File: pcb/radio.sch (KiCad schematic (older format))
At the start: 20 parts, among them IC401 Si4460, P401 COAX

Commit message: Work on schematic
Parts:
- removed Y?: TCXO 25MHz, Jerboa:ASTX_H11, symbol agg-kicad:TCXO
- added R? (x2): 100, symbol agg-kicad:R
- added R?: 68, symbol agg-kicad:R
- added R? (x2): 4k7, symbol agg-kicad:R
- added Y?: TCXO, Jerboa:ASTX_H11, symbol ASTX_H11:TCXO
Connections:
- net labels added: SI5351_3V3, WSPR_SCL, WSPR_SDA
- wire segments 44 -> 68
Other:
- moved on the sheet: U?
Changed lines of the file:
@@
 	6800 1850 7100 1850
-$Comp
-L agg-kicad:TCXO Y?
-U 1 1 5A7CB0D5
-P 3450 3850
-F 0 "Y?" H 3450 4075 50  0000 C CNN
-F 1 "TCXO 25MHz" H 3450 3984 50  0000 C CNN
-F 2 "Jerboa:ASTX_H11" H 3250 3850 50  0001 C CNN
-F 3 "" H 3250 3850 50  0001 C CNN
-F 4 "535-12039-1-ND" H 3450 3850 60  0001 C CNN "Digikey"
-	1    3450 3850
-	1    0    0    -1
-$EndComp
 $Comp
 L SI5351A_10_pin:SI5351A_10_pin U?
 U 1 1 5A7CC074
-P 4250 4200
-F 0 "U?" H 4750 4447 60  0000 C CNN
-F 1 "SI5351A_10_pin" H 4750 4341 60  0000 C CNN
-F 2 "" H 4250 4200 60  0001 C CNN
-F 3 "" H 4250 4200 60  0001 C CNN
-	1    4250 4200
+P 6600 4400
+F 0 "U?" H 7100 4647 60  0000 C CNN
+F 1 "SI5351A_10_pin" H 7100 4541 60  0000 C CNN
+F 2 "" H 6600 4400 60  0001 C CNN
+F 3 "" H 6600 4400 60  0001 C CNN
+	1    6600 4400
 	1    0    0    -1
 $EndComp
@@
 	1    0    0    -1
 $EndComp
+Text Label 6500 4350 2    60   ~ 0
+SI5351_3V3
+Text Label 2700 4100 0    60   ~ 0
+SI5351_3V3
+$Comp
+L ASTX_H11:TCXO Y?
+U 1 1 5A85FAB2
+P 5250 4800
+F 0 "Y?" H 5250 5025 50  0000 C CNN
+F 1 "TCXO" H 5250 4934 50  0000 C CNN
+F 2 "Jerboa:ASTX_H11" H 5250 4400 50  0001 C CNN
+F 3 "http://www.abracon.com/Oscillators/ASTX-H11.pdf" H 5250 4450 50  0001 C CNN
+F 4 "535-12039-1-ND" H 5050 4500 50  0001 L CNN "Digikey"
+	1    5250 4800
+	1    0    0    -1
+$EndComp
+Text Label 4900 4800 2    60   ~ 0
+SI5351_3V3
+Wire Wire Line
+	4900 4800 4950 4800
+Text Label 5650 5000 3    60   ~ 0
+SI5351_3V3
+$Comp
+L agg-kicad:R R?
+U 1 1 5A866FF6
+P 6200 4650
+F 0 "R?" V 6204 4691 50  0000 L CNN
+F 1 "100" V 6295 4691 50  0000 L CNN
+F 2 "" H 6200 4650 50  0001 C CNN
+F 3 "" H 6200 4650 50  0001 C CNN
+F 4 "Value" H 6200 4650 60  0001 C CNN "Farnell"
+	1    6200 4650
+	0    1    1    0
+$EndComp
+$Comp
+L agg-kicad:R R?
+U 1 1 5A867144
+P 6000 4800
+F 0 "R?" H 6050 4622 50  0000 C CNN
+F 1 "68" H 6050 4713 50  0000 C CNN
+F 2 "" H 6000 4800 50  0001 C CNN
+F 3 "" H 6000 4800 50  0001 C CNN
+F 4 "Value" H 6000 4800 60  0001 C CNN "Farnell"
+	1    6000 4800
+	-1   0    0    1
+$EndComp
+$Comp
+L agg-kicad:R R?
+U 1 1 5A8671A3
+P 5650 4650
+F 0 "R?" V 5654 4691 50  0000 L CNN
+F 1 "100" V 5745 4691 50  0000 L CNN
+F 2 "" H 5650 4650 50  0001 C CNN
+F 3 "" H 5650 4650 50  0001 C CNN
+F 4 "Value" H 5650 4650 60  0001 C CNN "Farnell"
+	1    5650 4650
+	0    1    1    0
+$EndComp
+Wire Wire Line
+	5550 4800 5900 4800
+Wire Wire Line
+	6000 4800 6600 4800
+Wire Wire Line
+	5650 4750 5650 4800
+Connection ~ 5650 4800
+Wire Wire Line
+	6200 4750 6200 4800
+Connection ~ 6200 4800
+Wire Wire Line
+	5550 4900 6600 4900
+$Comp
+L agg-kicad:GND #PWR?
+U 1 1 5A870B99
+P 5650 4600
+F 0 "#PWR?" H 5520 4640 50  0001 L CNN
+F 1 "GND" H 5650 4500 50  0000 C CNN
+F 2 "" H 5650 4600 60  0000 C CNN
+F 3 "" H 5650 4600 60  0000 C CNN
+	1    5650 4600
+	-1   0    0    1
+$EndComp
+$Comp
+L agg-kicad:GND #PWR?
+U 1 1 5A870C94
+P 6200 4600
+F 0 "#PWR?" H 6070 4640 50  0001 L CNN
+F 1 "GND" H 6200 4500 50  0000 C CNN
+F 2 "" H 6200 4600 60  0000 C CNN
+F 3 "" H 6200 4600 60  0000 C CNN
+	1    6200 4600
+	-1   0    0    1
+$EndComp
+Wire Wire Line
+	6200 4600 6200 4650
+Wire Wire Line
+	5650 4600 5650 4650
+$Comp
+L agg-kicad:GND #PWR?
+U 1 1 5A8745C5
+P 4900 4950
+F 0 "#PWR?" H 4770 4990 50  0001 L CNN
+F 1 "GND" H 4900 4850 50  0000 C CNN
+F 2 "" H 4900 4950 60  0000 C CNN
+F 3 "" H 4900 4950 60  0000 C CNN
+	1    4900 4950
+	1    0    0    -1
+$EndComp
+Wire Wire Line
+	4900 4950 4900 4900
+Wire Wire Line
+	4900 4900 4950 4900
+Wire Wire Line
+	6600 4500 6550 4500
+Wire Wire Line
+	6550 4350 6550 4500
+Wire Wire Line
+	6550 4400 6600 4400
+$Comp
+L agg-kicad:GND #PWR?
+U 1 1 5A8787FE
+P 6550 4650
+F 0 "#PWR?" H 6420 4690 50  0001 L CNN
+F 1 "GND" H 6550 4550 50  0000 C CNN
+F 2 "" H 6550 4650 60  0000 C CNN
+F 3 "" H 6550 4650 60  0000 C CNN
+	1    6550 4650
+	1    0    0    -1
+$EndComp
+Wire Wire Line
+	6550 4650 6550 4600
+Wire Wire Line
+	6550 4600 6600 4600
+Wire Wire Line
+	6500 4350 6550 4350
+Connection ~ 6550 4400
+$Comp
+L agg-kicad:R R?
+U 1 1 5A884D06
+P 6400 4950
+F 0 "R?" V 6404 4991 50  0000 L CNN
+F 1 "4k7" V 6495 4991 50  0000 L CNN
+F 2 "" H 6400 4950 50  0001 C CNN
+F 3 "" H 6400 4950 50  0001 C CNN
+F 4 "Value" H 6400 4950 60  0001 C CNN "Farnell"
+	1    6400 4950
+	0    1    1    0
+$EndComp
+$Comp
+L agg-kicad:R R?
+U 1 1 5A884DE4
+P 6400 5250
+F 0 "R?" V 6404 5291 50  0000 L CNN
+F 1 "4k7" V 6495 5291 50  0000 L CNN
+F 2 "" H 6400 5250 50  0001 C CNN
+F 3 "" H 6400 5250 50  0001 C CNN
+F 4 "Value" H 6400 5250 60  0001 C CNN "Farnell"
+	1    6400 5250
+	0    1    1    0
+$EndComp
+Wire Wire Line
+	6200 5100 6600 5100
+Connection ~ 6400 5100
+Wire Wire Line
+	6200 5200 6600 5200
+Connection ~ 6400 5200
+Wire Wire Line
+	6400 5050 6400 5100
+Wire Wire Line
+	5650 4950 6400 4950
+Wire Wire Line
+	6400 5250 6400 5200
+Wire Wire Line
+	6350 5350 6400 5350
+Text Label 6200 5200 2    60   ~ 0
+WSPR_SDA
+Text Label 6200 5100 2    60   ~ 0
+WSPR_SCL
+Wire Wire Line
+	5650 5000 5650 4900
+Connection ~ 5650 4900
+Connection ~ 5650 4950
+Wire Wire Line
+	6350 5350 6350 4950
+Connection ~ 6350 4950
 $EndSCHEMATC

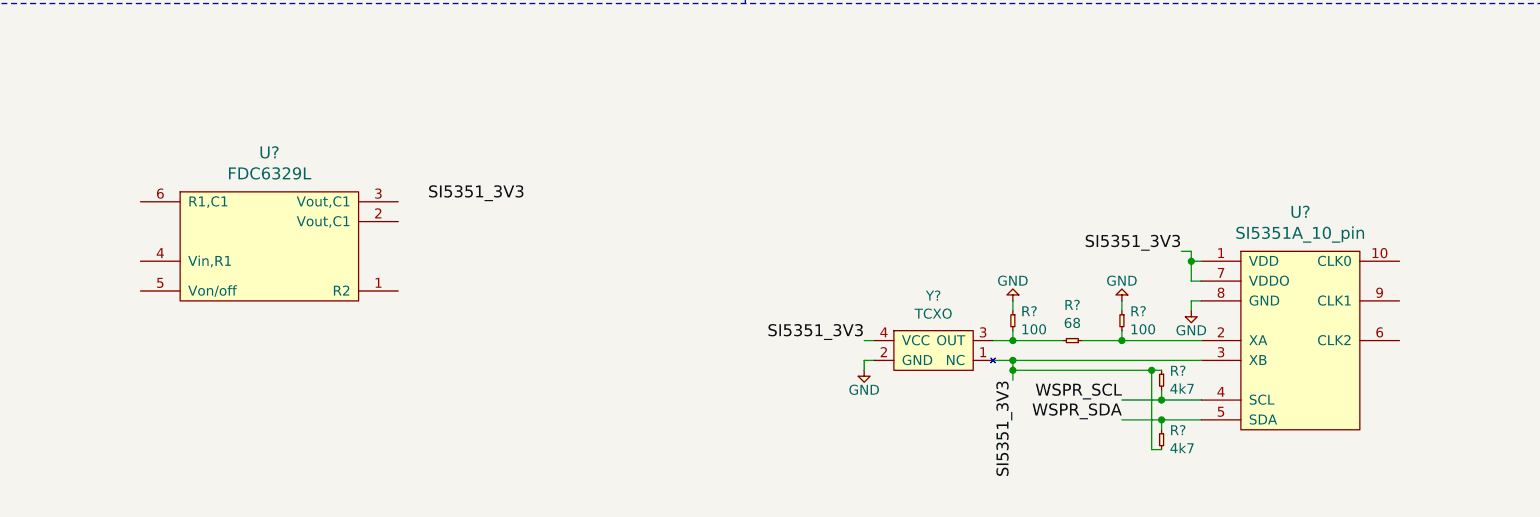
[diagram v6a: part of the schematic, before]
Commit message: Add wspr breakout board and reorganise sub project libraries
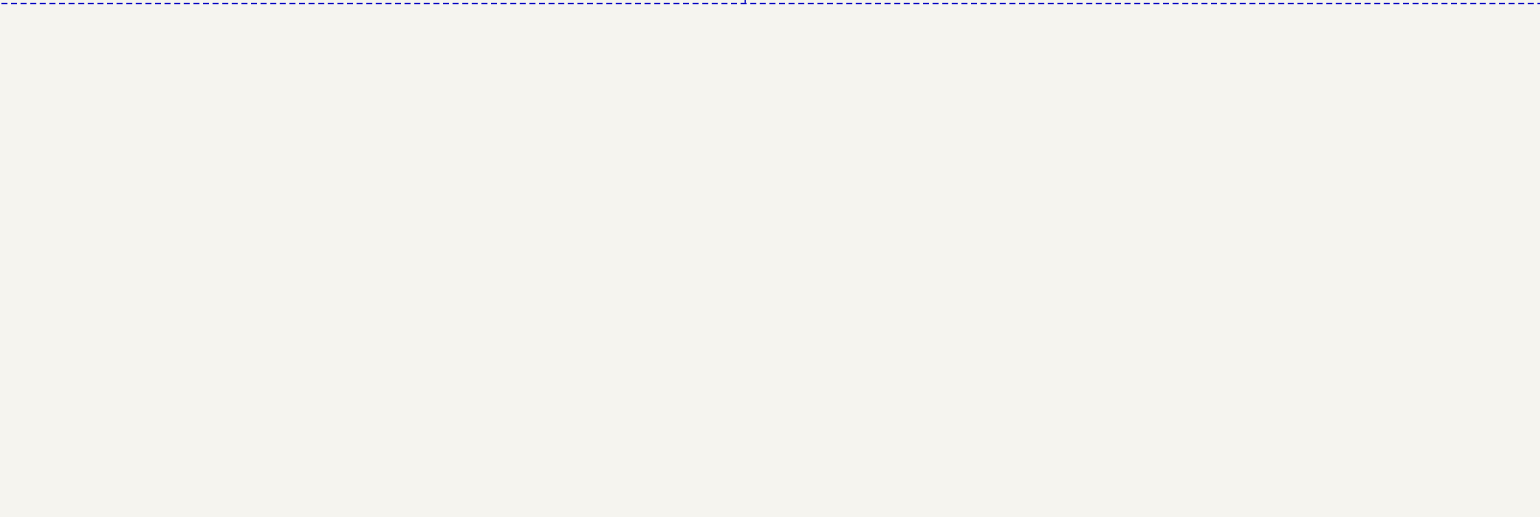
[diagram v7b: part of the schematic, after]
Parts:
- removed R? (x2): 100, symbol agg-kicad:R
- removed R?: 68, symbol agg-kicad:R
- removed R? (x2): 4k7, symbol agg-kicad:R
- removed U?: SI5351A_10_pin, symbol SI5351A_10_pin:SI5351A_10_pin
- removed U?: FDC6329L, Jerboa:SuperSOT-6, symbol FDC6329L:FDC6329L
- removed Y?: TCXO, Jerboa:ASTX_H11, symbol ASTX_H11:TCXO
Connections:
- net labels removed: SI5351_3V3, WSPR_SCL, WSPR_SDA
- wire segments 68 -> 44
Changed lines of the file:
@@
 Wire Wire Line
 	6800 1850 7100 1850
-$Comp
-L SI5351A_10_pin:SI5351A_10_pin U?
-U 1 1 5A7CC074
-P 6600 4400
-F 0 "U?" H 7100 4647 60  0000 C CNN
-F 1 "SI5351A_10_pin" H 7100 4541 60  0000 C CNN
-F 2 "" H 6600 4400 60  0001 C CNN
-F 3 "" H 6600 4400 60  0001 C CNN
-	1    6600 4400
-	1    0    0    -1
-$EndComp
-$Comp
-L FDC6329L:FDC6329L U?
-U 1 1 5A7E3431
-P 1900 4200
-F 0 "U?" H 1900 4547 60  0000 C CNN
-F 1 "FDC6329L" H 1900 4441 60  0000 C CNN
-F 2 "Jerboa:SuperSOT-6" H 1900 3550 60  0001 C CNN
-F 3 "http://www.farnell.com/datasheets/2285836.pdf" H 1900 3650 60  0001 C CNN
-F 4 "1652469" H 1900 3450 60  0001 C CNN "Farnell"
-	1    1900 4200
-	1    0    0    -1
-$EndComp
-Text Label 6500 4350 2    60   ~ 0
-SI5351_3V3
-Text Label 2700 4100 0    60   ~ 0
-SI5351_3V3
-$Comp
-L ASTX_H11:TCXO Y?
-U 1 1 5A85FAB2
-P 5250 4800
-F 0 "Y?" H 5250 5025 50  0000 C CNN
-F 1 "TCXO" H 5250 4934 50  0000 C CNN
-F 2 "Jerboa:ASTX_H11" H 5250 4400 50  0001 C CNN
-F 3 "http://www.abracon.com/Oscillators/ASTX-H11.pdf" H 5250 4450 50  0001 C CNN
-F 4 "535-12039-1-ND" H 5050 4500 50  0001 L CNN "Digikey"
-	1    5250 4800
-	1    0    0    -1
-$EndComp
-Text Label 4900 4800 2    60   ~ 0
-SI5351_3V3
-Wire Wire Line
-	4900 4800 4950 4800
-Text Label 5650 5000 3    60   ~ 0
-SI5351_3V3
-$Comp
-L agg-kicad:R R?
-U 1 1 5A866FF6
-P 6200 4650
-F 0 "R?" V 6204 4691 50  0000 L CNN
-F 1 "100" V 6295 4691 50  0000 L CNN
-F 2 "" H 6200 4650 50  0001 C CNN
-F 3 "" H 6200 4650 50  0001 C CNN
-F 4 "Value" H 6200 4650 60  0001 C CNN "Farnell"
-	1    6200 4650
-	0    1    1    0
-$EndComp
-$Comp
-L agg-kicad:R R?
-U 1 1 5A867144
-P 6000 4800
-F 0 "R?" H 6050 4622 50  0000 C CNN
-F 1 "68" H 6050 4713 50  0000 C CNN
-F 2 "" H 6000 4800 50  0001 C CNN
-F 3 "" H 6000 4800 50  0001 C CNN
-F 4 "Value" H 6000 4800 60  0001 C CNN "Farnell"
-	1    6000 4800
-	-1   0    0    1
-$EndComp
-$Comp
-L agg-kicad:R R?
-U 1 1 5A8671A3
-P 5650 4650
-F 0 "R?" V 5654 4691 50  0000 L CNN
-F 1 "100" V 5745 4691 50  0000 L CNN
-F 2 "" H 5650 4650 50  0001 C CNN
-F 3 "" H 5650 4650 50  0001 C CNN
-F 4 "Value" H 5650 4650 60  0001 C CNN "Farnell"
-	1    5650 4650
-	0    1    1    0
-$EndComp
-Wire Wire Line
-	5550 4800 5900 4800
-Wire Wire Line
-	6000 4800 6600 4800
-Wire Wire Line
-	5650 4750 5650 4800
-Connection ~ 5650 4800
-Wire Wire Line
-	6200 4750 6200 4800
-Connection ~ 6200 4800
-Wire Wire Line
-	5550 4900 6600 4900
-$Comp
-L agg-kicad:GND #PWR?
-U 1 1 5A870B99
-P 5650 4600
-F 0 "#PWR?" H 5520 4640 50  0001 L CNN
-F 1 "GND" H 5650 4500 50  0000 C CNN
-F 2 "" H 5650 4600 60  0000 C CNN
-F 3 "" H 5650 4600 60  0000 C CNN
-	1    5650 4600
-	-1   0    0    1
-$EndComp
-$Comp
-L agg-kicad:GND #PWR?
-U 1 1 5A870C94
-P 6200 4600
-F 0 "#PWR?" H 6070 4640 50  0001 L CNN
-F 1 "GND" H 6200 4500 50  0000 C CNN
-F 2 "" H 6200 4600 60  0000 C CNN
-F 3 "" H 6200 4600 60  0000 C CNN
-	1    6200 4600
-	-1   0    0    1
-$EndComp
-Wire Wire Line
-	6200 4600 6200 4650
-Wire Wire Line
-	5650 4600 5650 4650
-$Comp
-L agg-kicad:GND #PWR?
-U 1 1 5A8745C5
-P 4900 4950
-F 0 "#PWR?" H 4770 4990 50  0001 L CNN
-F 1 "GND" H 4900 4850 50  0000 C CNN
-F 2 "" H 4900 4950 60  0000 C CNN
-F 3 "" H 4900 4950 60  0000 C CNN
-	1    4900 4950
-	1    0    0    -1
-$EndComp
-Wire Wire Line
-	4900 4950 4900 4900
-Wire Wire Line
-	4900 4900 4950 4900
-Wire Wire Line
-	6600 4500 6550 4500
-Wire Wire Line
-	6550 4350 6550 4500
-Wire Wire Line
-	6550 4400 6600 4400
-$Comp
-L agg-kicad:GND #PWR?
-U 1 1 5A8787FE
-P 6550 4650
-F 0 "#PWR?" H 6420 4690 50  0001 L CNN
-F 1 "GND" H 6550 4550 50  0000 C CNN
-F 2 "" H 6550 4650 60  0000 C CNN
-F 3 "" H 6550 4650 60  0000 C CNN
-	1    6550 4650
-	1    0    0    -1
-$EndComp
-Wire Wire Line
-	6550 4650 6550 4600
-Wire Wire Line
-	6550 4600 6600 4600
-Wire Wire Line
-	6500 4350 6550 4350
-Connection ~ 6550 4400
-$Comp
-L agg-kicad:R R?
-U 1 1 5A884D06
-P 6400 4950
-F 0 "R?" V 6404 4991 50  0000 L CNN
-F 1 "4k7" V 6495 4991 50  0000 L CNN
-F 2 "" H 6400 4950 50  0001 C CNN
-F 3 "" H 6400 4950 50  0001 C CNN
-F 4 "Value" H 6400 4950 60  0001 C CNN "Farnell"
-	1    6400 4950
-	0    1    1    0
-$EndComp
-$Comp
-L agg-kicad:R R?
-U 1 1 5A884DE4
-P 6400 5250
-F 0 "R?" V 6404 5291 50  0000 L CNN
-F 1 "4k7" V 6495 5291 50  0000 L CNN
-F 2 "" H 6400 5250 50  0001 C CNN
-F 3 "" H 6400 5250 50  0001 C CNN
-F 4 "Value" H 6400 5250 60  0001 C CNN "Farnell"
-	1    6400 5250
-	0    1    1    0
-$EndComp
-Wire Wire Line
-	6200 5100 6600 5100
-Connection ~ 6400 5100
-Wire Wire Line
-	6200 5200 6600 5200
-Connection ~ 6400 5200
-Wire Wire Line
-	6400 5050 6400 5100
-Wire Wire Line
-	5650 4950 6400 4950
-Wire Wire Line
-	6400 5250 6400 5200
-Wire Wire Line
-	6350 5350 6400 5350
-Text Label 6200 5200 2    60   ~ 0
-WSPR_SDA
-Text Label 6200 5100 2    60   ~ 0
-WSPR_SCL
-Wire Wire Line
-	5650 5000 5650 4900
-Connection ~ 5650 4900
-Connection ~ 5650 4950
-Wire Wire Line
-	6350 5350 6350 4950
-Connection ~ 6350 4950
 $EndSCHEMATC

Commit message: Update clock input for clock buffer
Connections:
- wire segments 44 -> 66
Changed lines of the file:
@@
 $EndComp
 Wire Wire Line
-	900  1400 2250 1400
+	900  1400 1600 1400
 Wire Wire Line
 	1850 1700 1850 1600
@@
 Connection ~ 1850 1700
 Wire Wire Line
-	2050 1600 2050 1800
+	2050 1600 2050 1700
 Wire Wire Line
 	2250 1600 2150 1600
@@
 Connection ~ 2150 1400
 Wire Wire Line
-	2050 1300 2050 1500
+	2050 1300 2050 1400
 Wire Wire Line
 	1850 1400 1850 1500
@@
 	8150 2200 8150 2350
 Wire Wire Line
-	8150 2450 8150 2650
+	8150 2450 8150 2600
 Wire Wire Line
 	7750 2600 7750 2450
@@
 Connection ~ 6950 2600
 Wire Wire Line
-	8000 2200 8600 2200
-Wire Wire Line
-	7600 2200 7900 2200
+	8000 2200 8150 2200
+Wire Wire Line
+	7600 2200 7750 2200
 Wire Wire Line
 	7350 1850 7200 1850
@@
 $EndComp
 Wire Wire Line
-	6800 2200 7500 2200
+	6800 2200 6950 2200
 Wire Wire Line
 	6950 2350 6950 2200
 Wire Wire Line
-	6400 2600 7100 2600
-Wire Wire Line
-	6400 2200 6700 2200
-Wire Wire Line
-	7200 2600 8600 2600
+	6400 2600 6550 2600
+Wire Wire Line
+	6400 2200 6550 2200
+Wire Wire Line
+	7200 2600 7350 2600
 Wire Wire Line
 	6550 1700 6550 1850
 Wire Wire Line
-	6400 1850 6700 1850
-Wire Wire Line
-	7350 1850 7350 2350
+	6400 1850 6550 1850
+Wire Wire Line
+	7350 1850 7350 2200
 Connection ~ 6550 2200
 Connection ~ 6550 2600
@@
 RADIO_nIRQ
 Wire Wire Line
-	1600 1700 2250 1700
+	1600 1700 1850 1700
 Wire Wire Line
 	6800 1850 7100 1850
+Wire Wire Line
+	2050 1700 2050 1800
+Wire Wire Line
+	2050 1700 2150 1700
+Wire Wire Line
+	1850 1700 2050 1700
+Wire Wire Line
+	2150 1700 2250 1700
+Wire Wire Line
+	2150 1400 2250 1400
+Wire Wire Line
+	2050 1400 2150 1400
+Wire Wire Line
+	2050 1400 2050 1500
+Wire Wire Line
+	1850 1400 2050 1400
+Wire Wire Line
+	1600 1400 1850 1400
+Wire Wire Line
+	7750 2600 8150 2600
+Wire Wire Line
+	7750 2200 7900 2200
+Wire Wire Line
+	8150 2600 8150 2650
+Wire Wire Line
+	8150 2600 8600 2600
+Wire Wire Line
+	7350 2200 7500 2200
+Wire Wire Line
+	7350 2200 7350 2350
+Wire Wire Line
+	6550 1850 6700 1850
+Wire Wire Line
+	6950 2200 7350 2200
+Wire Wire Line
+	7350 2600 7750 2600
+Wire Wire Line
+	6950 2600 7100 2600
+Wire Wire Line
+	8150 2200 8600 2200
+Wire Wire Line
+	6550 2200 6700 2200
+Wire Wire Line
+	6550 2600 6950 2600
 $EndSCHEMATC
